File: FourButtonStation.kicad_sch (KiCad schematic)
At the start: 41 parts, among them J1 c8-inlet, J2 Conn_WallSocket, J3 I2C, J4 AVOX Adapter, J5 Conn_WallSocket, J6 USB_B_Micro, J7 Conn_WallSocket, J8 Conn_WallSocket, J9 I2C, K1 G5Q-1, K2 G5Q-1, K4 FINDER-36.11, K5 G5Q-1, Q1 MMBT3904, Q2 MMBT3904, Q3 MMBT3904, Q4 MMBT3904, Q5 MMBT3904, Q6 MMBT3904, SW3 RST, SW4 Boot, U1 CH340C, U2 radio-receiver, U3 ESP-07

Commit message: Schematic and routing
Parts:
- removed C1: TODO: 20u as SMD Package?, Capacitor_THT:CP_Radial_D5.0mm_P2.50mm, symbol Device:C_Polarized_Small
- removed D1: TODO: SMD Diodes Package, Diode_THT:D_DO-15_P2.54mm_Vertical_KathodeUp, symbol Device:D_Small
- removed D2, D3, D4: D_Small, Diode_THT:D_DO-15_P2.54mm_Vertical_KathodeUp, symbol Device:D_Small
- removed J2: Conn_WallSocket, TerminalBlock_Phoenix:TerminalBlock_Phoenix_MKDS-1,5-2_1x02_P5.00mm_Horizontal, symbol Connector:Conn_WallSocket
- removed J9: I2C, jlc_footprints:CONN-SMD_BM04B-SRSS-TB, symbol BM04B-SRSS-TB(LF)(SN):BM04B-SRSS-TB(LF)(SN)
- removed K1, K2, K5: G5Q-1, omron-g5sb-14:RELAY_G5SB-14_OMR, symbol Relay:G5Q-1
- removed K4: FINDER-36.11, omron-g5sb-14:RELAY_G5SB-14_OMR, symbol Relay:FINDER-36.11
- removed Q2, Q4, Q5, Q6: MMBT3904, jlc_footprints:SOT-23-3_L2.9-W1.3-P1.90-LS2.4-BR, symbol Transistor_BJT:MMBT3904
- removed R1: 33k, Resistor_SMD:R_0603_1608Metric_Pad0.98x0.95mm_HandSolder, symbol Device:R
- removed R4, R5, R6: TODO: 33k needs to be JLC Package, Resistor_SMD:R_0603_1608Metric_Pad0.98x0.95mm_HandSolder, symbol Device:R
- removed SW3: RST, jlc_footprints:SW-SMD_4P-L5.1-W5.1-P3.70-LS6.5-TL-2, symbol Switch:SW_Push
- removed SW4: Boot, jlc_footprints:SW-SMD_4P-L5.1-W5.1-P3.70-LS6.5-TL-2, symbol Switch:SW_Push
- added J10: AC IN, TerminalBlock_Phoenix:TerminalBlock_Phoenix_MKDS-1,5-2_1x02_P5.00mm_Horizontal, symbol Connector:Screw_Terminal_01x02
- added J2: External 3V, Connector_PinHeader_2.54mm:PinHeader_1x02_P2.54mm_Vertical, symbol Connector_Generic:Conn_01x02
- added J9: Conn_WallSocket, TerminalBlock_Phoenix:TerminalBlock_Phoenix_MKDS-1,5-2_1x02_P5.00mm_Horizontal, symbol Connector:Conn_WallSocket
- added K1, K2, K3, K4: G5LE-1, Relay_THT:Relay_SPDT_Omron-G5LE-1, symbol Relay:G5LE-1
- added LED1, LED2, LED3, LED4: KT-0603R, jlc_footprints:LED0603-RD, symbol jlc_symbols:KT-0603R
- added R1, R10, R6, R8: 33k, jlc_footprints:R0603, symbol jlc_symbols:0603WAF3302T5E
- added R4, R5, R7, R9: 1k, jlc_footprints:R0603, symbol jlc_symbols:0603WAF3302T5E
- added SW1: POWER, as12ap:as12ap, symbol Switch:SW_SPDT
- added SW2: RST, jlc_footprints:SW-SMD_4P-L5.1-W5.1-P3.70-LS6.5-TL-2, symbol TS-1187A-B-A-B:TS-1187A-B-A-B
- added SW5: Mode, jlc_footprints:SW-SMD_4P-L5.1-W5.1-P3.70-LS6.5-TL-2, symbol TS-1187A-B-A-B:TS-1187A-B-A-B
- added U10, U4, U6, U8: SM4007PL, jlc_footprints:SOD-123F_L2.8-W1.8-LS3.7-RD, symbol jlc_symbols:SM4007PL
- added U11, U5, U7, U9: D882_C9634, jlc_footprints:SOT-89-3_L4.5-W2.5-P1.50-LS4.2-BR, symbol jlc_symbols:D882_C9634
- J1: value c8-inlet -> AC IN; now left out of the parts list
- J3: value I2C -> TTL
- J4: value AVOX Adapter -> TODO: AVOX Adapter might need voltage divider
- J6: footprint Connector_USB:USB_Micro-B_Molex-105017-0001 -> jlc_footprints:MICRO-USB-SMD_1050171001
- R2, R3: footprint jlc_footprints:C0402 -> jlc_footprints:R0402
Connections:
- net +3V3: now also J3.4 (Pin_4), J4.3 (Pin_3), K1.5, K2.5, K3.5, K4.5, LED1.2 (A), LED2.2 (A), LED3.2 (A), LED4.2 (A), SW1.2 (B), U10.1 (C), U4.1 (C), U6.1 (C), U8.1 (C); no longer J3.2 (Pin_2), J4.1 (Pin_1), PS1.4 (+Vo)
- net AC1: now also K1.3
- net AC2: now also J7.1 (AC_P), K2.3
- net AC3: now also J8.1 (AC_P), K3.3; no longer J7.1 (AC_P)
- net AC4: now also J9.1 (AC_P), K4.3; no longer J8.1 (AC_P)
- net ADC: now also J4.2 (Pin_2); no longer J4.3 (Pin_3)
- net GND: now also J4.1 (Pin_1), J2.1 (Pin_1), SW2.3 (C), SW5.3 (C), U11.3 (E), U5.3 (E), U7.3 (E), U9.3 (E); no longer J4.2 (Pin_2)
- net GPIO0: now also U3.12 (GPIO0), SW5.1 (A)
- net Nullleiter: now also J10.1 (Pin_1), J9.2 (AC_N)
- net Phase: now also J10.2 (Pin_2), K1.1, K2.1, K3.1, K4.1
- net RESET: now also U3.1 (~{RST}), SW2.1 (A)
- net RX: now also J3.3 (Pin_3), U3.15 (GPIO3/RXD); no longer U3.16 (GPIO1/TXD)
- net RadioA: now also U3.13 (GPIO4)
- net RadioB: now also U3.11 (GPIO2)
- net RadioC: now also U3.10 (GPIO15); no longer U3.13 (GPIO4)
- net RadioD: now also U3.7 (GPIO13); no longer U3.11 (GPIO2)
- net Relay1: now also R1.1
- net Relay2: now also R6.1
- net Relay3: now also R8.1
- net Relay4: now also R10.1
- net TX: now also J3.2 (Pin_2), U3.16 (GPIO1/TXD); no longer U3.15 (GPIO3/RXD)
- removed net SCL: J3.4 (Pin_4), U3.10 (GPIO15)
- removed net SDA: J3.3 (Pin_3), U3.7 (GPIO13)
- new net: R1.2, U5.1 (B)
- new net: K4.2, R9.1, U10.2 (A), U11.2 (C)
- new net: LED4.1 (K), R9.2
- new net: LED2.1 (K), R5.2
- new net: R10.2, U11.1 (B)
- new net: LED3.1 (K), R7.2
- new net: K1.2, R4.1, U4.2 (A), U5.2 (C)
- new net: R6.2, U7.1 (B)
- new net: K2.2, R5.1, U6.2 (A), U7.2 (C)
- new net: K3.2, R7.1, U8.2 (A), U9.2 (C)
- new net: LED1.1 (K), R4.2
- new net: PS1.4 (+Vo), SW1.1 (A)
- new net: R8.2, U9.1 (B)
- new net POWX: J2.2 (Pin_2), SW1.3 (C)
- no-connect marks 12 -> 16
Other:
- note added: "Relay: G5LE14 3V Adafruit uses it: https://www.digikey.ch/de/products/detail/adafruit-industries-llc/3191/6193590 Footprint JLC C688864 (songle version)"
- note added: "TODO: - Exclude all from BOM what I will place my self - Add a warning sign - Add capacitors for 3v3"
- note removed: "TODO: - Add antenna to button module"
- moved on the sheet: J5

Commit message: Prepare for production
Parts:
- added C1, C6: 10u, jlc_footprints:C0402, symbol CL05A106MQ5NUNC:CL05A106MQ5NUNC
- added C2, C5: 100n, jlc_footprints:C0402, symbol CL05B104KO5NNNC:CL05B104KO5NNNC
- added C3: 22u, jlc_footprints:C0603, symbol CL10A226MQ8NRNC:CL10A226MQ8NRNC
- added C4: 100u, jlc_footprints:C1206, symbol CL31A107MQHNNNE:CL31A107MQHNNNE
- added R11: 22k, jlc_footprints:R0603, symbol jlc_symbols:0603WAF2202T5E
- added R12: 10k, jlc_footprints:R0603, symbol jlc_symbols:0603WAF1002T5E
- added SYM1: SYM_Flash_XLarge, Symbol:Symbol_HighVoltage_Type2_CopperTop_VerySmall, symbol Graphic:SYM_Flash_XLarge
- added Sym2: github.com/besi/four-button-station, Symbol:OSHW-Symbol_6.7x6mm_SilkScreen, symbol Graphic:Logo_Open_Hardware_Small
- added Sym3: SYM_Flash_XLarge, Symbol:EasterEgg_EWG1308-2013_ClassA, symbol Graphic:SYM_Flash_XLarge
- added U13: AMS1117-3_3, jlc_footprints:SOT-223-3_L6.5-W3.4-P2.30-LS7.0-BR, symbol jlc_symbols:AMS1117-3_3
- F1, H1, H2, H3, H4, J2, J5, J7, J8, J9, K1, K2, K3, K4, PS1, SW1, U2: now left out of the parts list
- J3: value TTL -> UART; now left out of the parts list
- J4: value TODO: AVOX Adapter might need voltage divider -> ADC; now left out of the parts list
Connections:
- net +3V3: now also C4.2, C5.2, C6.2
- net AC_FUSE: now also J10.1 (Pin_1)
- net ADC: now also R11.1, R12.2; no longer J4.2 (Pin_2)
- net GND: now also C1.1, C2.1, C3.1, C4.1, C5.1, C6.1, R12.1, U13.1 (GND)
- net Nullleiter: no longer J10.1 (Pin_1)
- net POWX renamed POW3V3
- net POW3V3: now also U13.2 (VOUT), U13.4 (VOUT)
- net VBUS renamed +5V
- net +5V: now also C1.2, C2.2, C3.2, U13.3 (VIN)
- new net: J4.2 (Pin_2), R11.2
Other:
- note added: "TODO: - ADC can be used as helligkeits dinsg oder TCRT5000 - PCB Artwork - QRCODE of project - Tidy up"
- note removed: "Relay: G5LE14 3V Adafruit uses it: https://www.digikey.ch/de/products/detail/adafruit-industries-llc/3191/6193590 Footprint JLC C688864 (songle version)"
- note removed: "TODO: - Exclude all from BOM what I will place my self - Add a warning sign - Add capacitors for 3v3"
- moved on the sheet: F1, H1, H2, H3, H4, J1, J10, J2, J4, PS1, U2, U3

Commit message: Production files for 2.0
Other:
- title: (none) -> FourButtonStation
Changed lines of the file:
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@@
 (kicad_sch (version 20230121) (generator eeschema)
   (paper "A4")
+  (title_block
+    (title "FourButtonStation")
+    (date "2024-03-11")
+    (rev "2.0 - aa14c0")
+  )
   (junction (at 365.76 143.51) (diameter 0) (color 0 0 0 0)
   )

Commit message: Update version
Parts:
- SYM1: footprint Symbol:Symbol_HighVoltage_Type2_CopperTop_VerySmall -> (none)
- Sym3: footprint Symbol:EasterEgg_EWG1308-2013_ClassA -> (none)
- renumbered Sym2 to Logo1
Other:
- note added: "Microcontroller"
- note added: "Peripherals"
- note added: "Power"
- note added: "Relays"
- note removed: "TODO: - ADC can be used as helligkeits dinsg oder TCRT5000 - PCB Artwork - QRCODE of project - Tidy up"
- note removed: "TODO: First needs to be tested in Stepomatic"
- moved on the sheet: C1, C2, C3, C4, C5, C6, F1, H1, H2, H3, H4, J1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

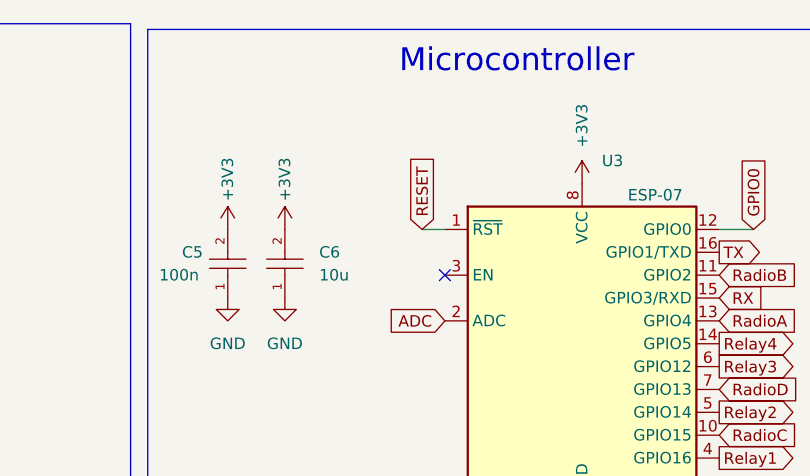
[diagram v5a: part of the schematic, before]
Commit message: Add 10k pull up for enabling the esp
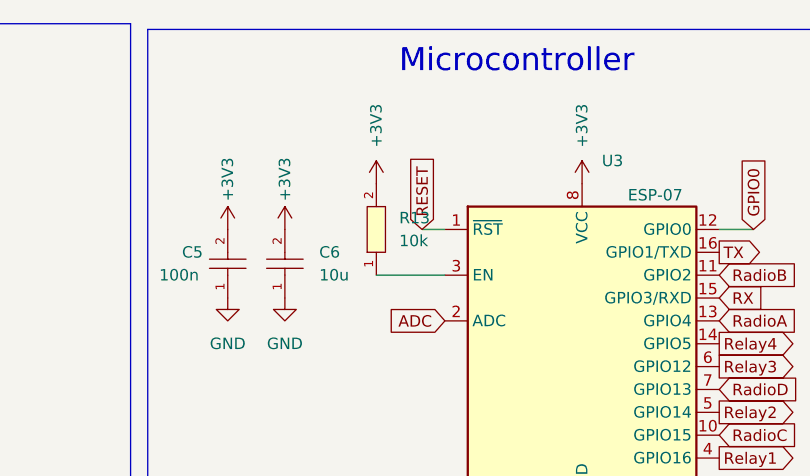
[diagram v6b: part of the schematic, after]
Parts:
- added R13: 10k, jlc_footprints:R0603, symbol jlc_symbols:0603WAF1002T5E
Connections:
- net +3V3: now also R13.2
- net at U3.3 (EN): now also R13.1
- no-connect marks 16 -> 15
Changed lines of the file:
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@@
   (no_connect (at 209.55 112.395))
   (no_connect (at 118.11 107.95))
-  (no_connect (at 226.06 41.91))
   (no_connect (at 229.87 122.555))
   (no_connect (at 229.87 125.095))
@@
     (stroke (width 0) (type default))
   )
+  (wire (pts (xy 218.44 41.91) (xy 226.06 41.91))
+    (stroke (width 0) (type default))
+  )
   (wire (pts (xy 27.305 27.305) (xy 34.925 27.305))
     (stroke (width 0) (type default))
@@
         (path "/fe8954b5-d30a-4533-a19e-bff77a7cd4d5"
           (reference "#PWR016") (unit 1)
+        )
+      )
+    )
+  )
+  (symbol (lib_id "jlc_symbols:0603WAF1002T5E") (at 218.44 36.83 90) (unit 1)
+    (in_bom yes) (on_board yes) (dnp no) (fields_autoplaced)
+    (property "Reference" "R13" (at 220.98 35.56 90)
+      (effects (font (size 1.27 1.27)) (justify right))
+    )
+    (property "Value" "10k" (at 220.98 38.1 90)
+      (effects (font (size 1.27 1.27)) (justify right))
+    )
+    (property "Footprint" "jlc_footprints:R0603" (at 228.6 36.83 0)
+      (effects (font (size 1.27 1.27) italic) hide)
+    )
+    (property "Datasheet" "https://www.mouser.in/datasheet/2/447/PYu_RT_1_to_0_01_RoHS_L_11-1669912.pdf" (at 218.313 39.116 0)
+      (effects (font (size 1.27 1.27)) (justify left) hide)
+    )
+    (property "LCSC" "C25804" (at 218.44 36.83 0)
+      (effects (font (size 1.27 1.27)) hide)
+    )
+    (pin "1")
+    (pin "2")
+    (instances
+      (project "FourButtonStation"
+        (path "/fe8954b5-d30a-4533-a19e-bff77a7cd4d5"
+          (reference "R13") (unit 1)
         )
       )
@@
         )
       )
+    )
+  )
+  (symbol (lib_id "power:+3V3") (at 218.44 31.75 0) (unit 1)
+    (in_bom yes) (on_board yes) (dnp no)
+    (property "Reference" "#PWR040" (at 218.44 35.56 0)
+      (effects (font (size 1.27 1.27)) hide)
+    )
+    (property "Value" "+3V3" (at 218.44 22.86 90)
+      (effects (font (size 1.27 1.27)) (justify right))
+    )
+    (property "Footprint" "" (at 218.44 31.75 0)
+      (effects (font (size 1.27 1.27)) hide)
+    )
+    (property "Datasheet" "" (at 218.44 31.75 0)
+      (effects (font (size 1.27 1.27)) hide)
+    )
+    (pin "1")
+    (instances
+      (project "FourButtonStation"
+        (path "/fe8954b5-d30a-4533-a19e-bff77a7cd4d5"
+          (reference "#PWR040") (unit 1)
+        )
+      )

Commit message: Update schematic
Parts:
- added C7: 1u, jlc_footprints:C0603, symbol jlc_symbols:CL10A105KB8NNNC
- added R14: 10k, jlc_footprints:R0603, symbol jlc_symbols:0603WAF1002T5E
- J1: footprint c8-inlet:c8-inlet -> c8-inlet:c8-inlet-old
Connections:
- net GND: now also C7.1, R14.1
- net RadioC: now also R14.2
- net at R13.1, U3.3 (EN): now also C7.2
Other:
- note added: "TODO: Pulldown on GPIO15"
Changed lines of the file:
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@@
   (junction (at 121.285 72.39) (diameter 0) (color 0 0 0 0)
   )
+  (junction (at 267.97 59.69) (diameter 0) (color 0 0 0 0)
+  )
   (junction (at 43.815 159.385) (diameter 0) (color 0 0 0 0)
   )
@@
   (junction (at 34.925 90.805) (diameter 0) (color 0 0 0 0)
   )
+  (junction (at 218.44 41.91) (diameter 0) (color 0 0 0 0)
+  )
   (junction (at 100.965 38.735) (diameter 0) (color 0 0 0 0)
   )
@@
     (stroke (width 0) (type default))
   )
+  (wire (pts (xy 267.97 59.69) (xy 270.51 59.69))
+    (stroke (width 0) (type default))
+  )
   (wire (pts (xy 43.815 69.215) (xy 43.815 70.485))
     (stroke (width 0) (type default))
@@
     (stroke (width 0) (type default))
   )
+  (wire (pts (xy 256.54 59.69) (xy 267.97 59.69))
+    (stroke (width 0) (type default))
+  )
   (wire (pts (xy 117.475 38.735) (xy 123.825 38.735))
     (stroke (width 0) (type default))
@@
     (effects (font (size 2.54 2.54)) (justify left bottom))
   )
+  (text "TODO: Pulldown on GPIO15\n" (at 304.8 57.15 0)
+    (effects (font (size 2.54 2.54)) (justify left bottom))
+  )
   (label "Nullleiter" (at 66.675 93.345 180) (fields_autoplaced)
     (effects (font (size 1.27 1.27)) (justify right bottom))
@@
     )
   )
-  (global_label "RadioC" (shape input) (at 256.54 59.69 0) (fields_autoplaced)
+  (global_label "RadioC" (shape input) (at 270.51 59.69 0) (fields_autoplaced)
     (effects (font (size 1.27 1.27)) (justify left))
-    (property "Intersheetrefs" "${INTERSHEET_REFS}" (at 265.545 59.7694 0)
+    (property "Intersheetrefs" "${INTERSHEET_REFS}" (at 279.515 59.7694 0)
       (effects (font (size 1.27 1.27)) (justify left) hide)
     )
@@
     )
   )
+  (symbol (lib_id "power:GND") (at 218.44 52.07 0) (unit 1)
+    (in_bom yes) (on_board yes) (dnp no)
+    (property "Reference" "#PWR042" (at 218.44 58.42 0)
+      (effects (font (size 1.27 1.27)) hide)
+    )
+    (property "Value" "GND" (at 218.44 59.69 90)
+      (effects (font (size 1.27 1.27)) (justify left))
+    )
+    (property "Footprint" "" (at 218.44 52.07 0)
+      (effects (font (size 1.27 1.27)) hide)
+    )
+    (property "Datasheet" "" (at 218.44 52.07 0)
+      (effects (font (size 1.27 1.27)) hide)
+    )
+    (pin "1")
+    (instances
+      (project "FourButtonStation"
+        (path "/fe8954b5-d30a-4533-a19e-bff77a7cd4d5"
+          (reference "#PWR042") (unit 1)
+        )
+      )
+    )
+  )
   (symbol (lib_id "Graphic:SYM_Flash_XLarge") (at 80.645 110.49 0) (unit 1)
     (in_bom no) (on_board no) (dnp no) (fields_autoplaced)
@@
     )
   )
+  (symbol (lib_id "jlc_symbols:0603WAF1002T5E") (at 267.97 64.77 90) (unit 1)
+    (in_bom yes) (on_board yes) (dnp no) (fields_autoplaced)
+    (property "Reference" "R14" (at 270.51 63.5 90)
+      (effects (font (size 1.27 1.27)) (justify right))
+    )
+    (property "Value" "10k" (at 270.51 66.04 90)
+      (effects (font (size 1.27 1.27)) (justify right))
+    )
+    (property "Footprint" "jlc_footprints:R0603" (at 278.13 64.77 0)
+      (effects (font (size 1.27 1.27) italic) hide)
+    )
+    (property "Datasheet" "https://www.mouser.in/datasheet/2/447/PYu_RT_1_to_0_01_RoHS_L_11-1669912.pdf" (at 267.843 67.056 0)
+      (effects (font (size 1.27 1.27)) (justify left) hide)
+    )
+    (property "LCSC" "C25804" (at 267.97 64.77 0)
+      (effects (font (size 1.27 1.27)) hide)
+    )
+    (pin "1")
+    (pin "2")
+    (instances
+      (project "FourButtonStation"
+        (path "/fe8954b5-d30a-4533-a19e-bff77a7cd4d5"
+          (reference "R14") (unit 1)
+        )
+      )
+    )
+  )
   (symbol (lib_id "Transistor_BJT:MMBT3904") (at 254 127.635 180) (unit 1)
     (in_bom yes) (on_board yes) (dnp no) (fields_autoplaced)
@@
   )
   (symbol (lib_id "CL05A106MQ5NUNC:CL05A106MQ5NUNC") (at 208.28 40.64 90) (unit 1)
-    (in_bom yes) (on_board yes) (dnp no) (fields_autoplaced)
-    (property "Reference" "C6" (at 212.09 39.3699 90)
+    (in_bom yes) (on_board yes) (dnp no)
+    (property "Reference" "C6" (at 210.82 39.37 90)
       (effects (font (size 1.27 1.27)) (justify right))
     )
-    (property "Value" "10u" (at 212.09 41.9099 90)
+    (property "Value" "10u" (at 210.82 41.91 90)
       (effects (font (size 1.27 1.27)) (justify right))
     )
@@
     )
   )
+  (symbol (lib_id "jlc_symbols:CL10A105KB8NNNC") (at 218.44 46.99 90) (unit 1)
+    (in_bom yes) (on_board yes) (dnp no)
+    (property "Reference" "C7" (at 213.36 45.72 90)
+      (effects (font (size 1.27 1.27)) (justify right))
+    )
+    (property "Value" "1u" (at 213.36 48.26 90)
+      (effects (font (size 1.27 1.27)) (justify right))
+    )
+    (property "Footprint" "jlc_footprints:C0603" (at 228.6 46.99 0)
+      (effects (font (size 1.27 1.27) italic) hide)
+    )
+    (property "Datasheet" "https://item.szlcsc.com/362304.html" (at 218.313 49.276 0)
+      (effects (font (size 1.27 1.27)) (justify left) hide)
+    )
+    (property "LCSC" "C15849" (at 218.44 46.99 0)
+      (effects (font (size 1.27 1.27)) hide)
+    )
+    (pin "2")
+    (pin "1")
+    (instances
+      (project "FourButtonStation"
+        (path "/fe8954b5-d30a-4533-a19e-bff77a7cd4d5"
+          (reference "C7") (unit 1)
+        )
+      )
+    )
+  )
   (symbol (lib_id "jlc_symbols:SM4007PL") (at 34.925 168.275 270) (unit 1)
     (in_bom yes) (on_board yes) (dnp no)
@@
       (effects (font (size 1.27 1.27)) (justify right))
     )
-    (property "Footprint" "c8-inlet:c8-inlet" (at 117.1194 63.1952 0)
+    (property "Footprint" "c8-inlet:c8-inlet-old" (at 117.1194 63.1952 0)
       (effects (font (size 1.27 1.27)) hide)
     )
@@
         )
       )
+    )
+  )
+  (symbol (lib_id "power:GND") (at 267.97 69.85 0) (unit 1)
+    (in_bom yes) (on_board yes) (dnp no)
+    (property "Reference" "#PWR041" (at 267.97 76.2 0)
+      (effects (font (size 1.27 1.27)) hide)
+    )
+    (property "Value" "GND" (at 267.97 77.47 90)
+      (effects (font (size 1.27 1.27)) (justify left))
+    )
+    (property "Footprint" "" (at 267.97 69.85 0)
+      (effects (font (size 1.27 1.27)) hide)
+    )
+    (property "Datasheet" "" (at 267.97 69.85 0)
+      (effects (font (size 1.27 1.27)) hide)
+    )
+    (pin "1")
+    (instances
+      (project "FourButtonStation"
+        (path "/fe8954b5-d30a-4533-a19e-bff77a7cd4d5"
+          (reference "#PWR041") (unit 1)
+        )
+      )
